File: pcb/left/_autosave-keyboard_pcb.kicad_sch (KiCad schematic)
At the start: 44 parts, among them J1 TRRS, J2 Conn_01x04_Male, K0 KEYSW, K1 KEYSW, K10 KEYSW, K11 KEYSW, K12 KEYSW, K13 KEYSW, K14 KEYSW, K15 KEYSW, K2 KEYSW, K20 KEYSW, K21 KEYSW, K22 KEYSW, K23 KEYSW, K24 KEYSW, K25 KEYSW, K3 KEYSW, K30 KEYSW, K31 KEYSW, K32 KEYSW, K4 KEYSW, K5 KEYSW, U1 PCF8574, U2 Pico

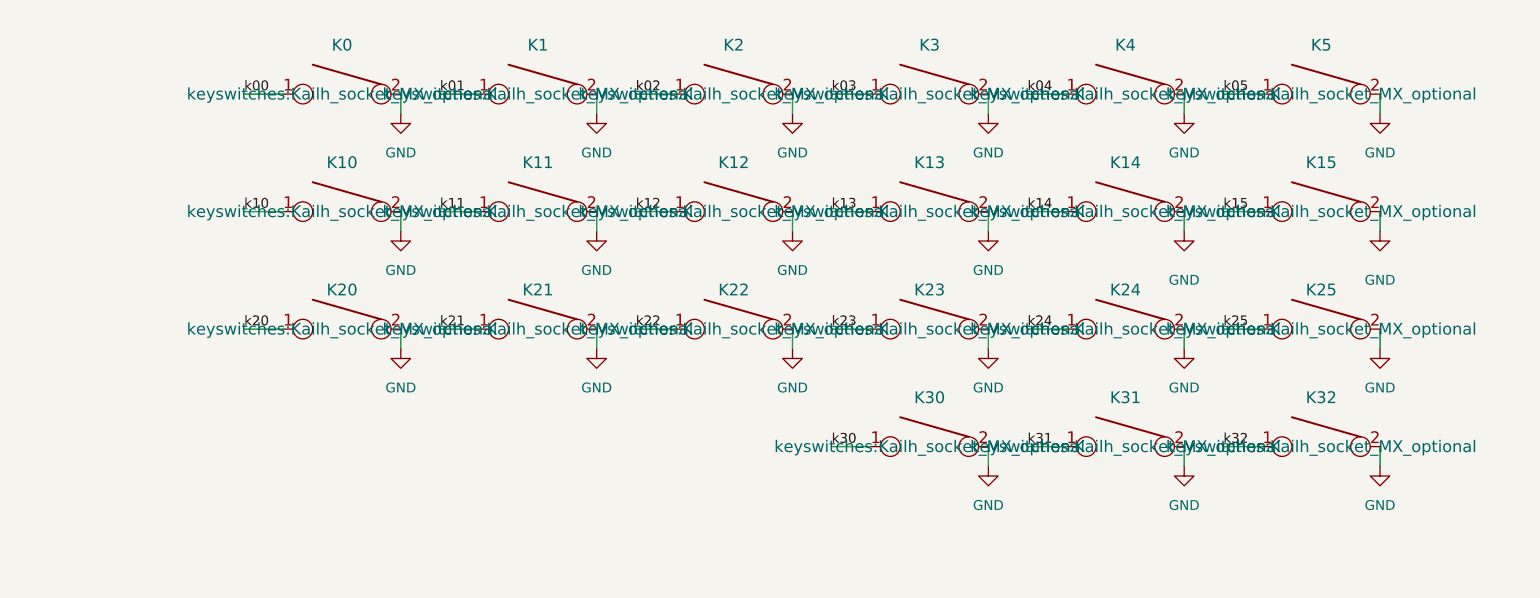
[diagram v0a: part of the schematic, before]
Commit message: Now there are MX switches on the pcb, 3d check via printing the pcb and populating the switches with caps
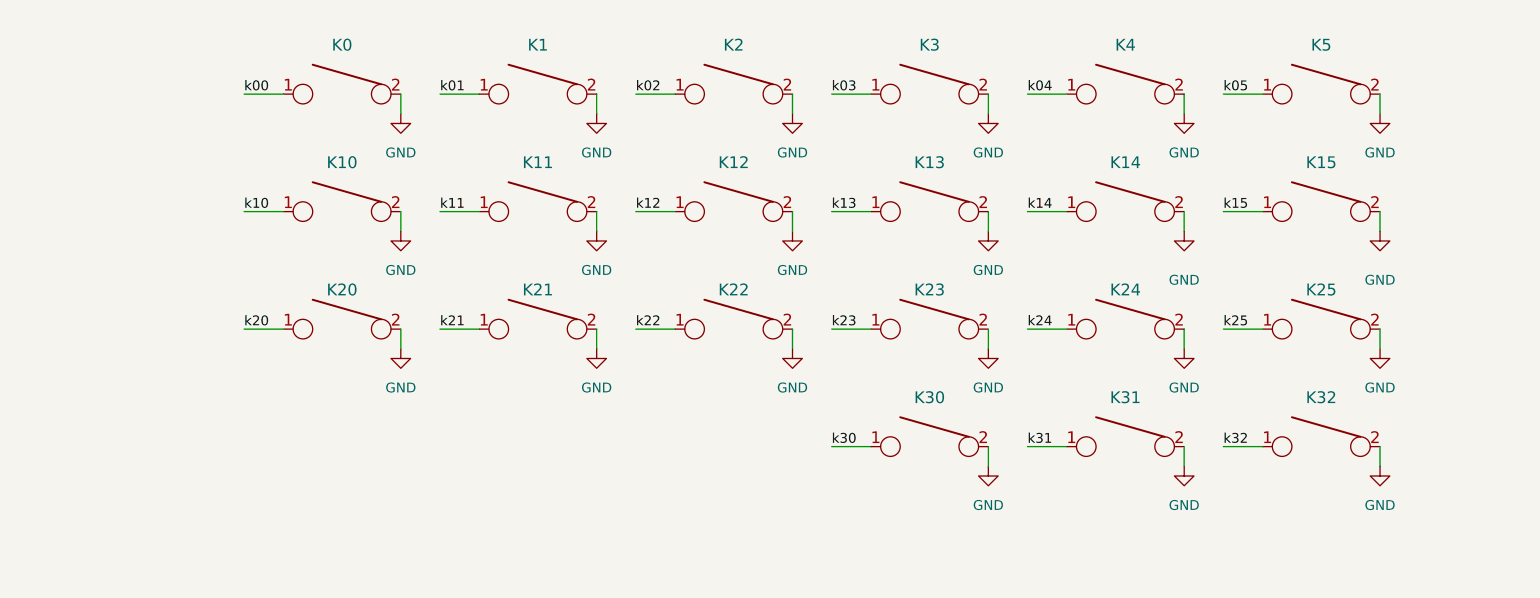
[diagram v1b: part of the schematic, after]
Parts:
- D1, D2: footprint LED_SMD:LED_0603_1608Metric -> (none)
- J1: footprint trrs_audiojack:TRRS-PJ-320A_fab -> trrs_audiojack:TRRS-PJ-320A
- K0, K1, K10, K11, K12, K13, K14, K15, K2, K20, K21, K22, K23, K24, K25, K3, K30, K31, K32, K4, K5: footprint keyswitches:Kailh_socket_MX_optional_platemount -> keyswitches:Kailh_socket_MX_optional
